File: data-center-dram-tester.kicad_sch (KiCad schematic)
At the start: 6 parts

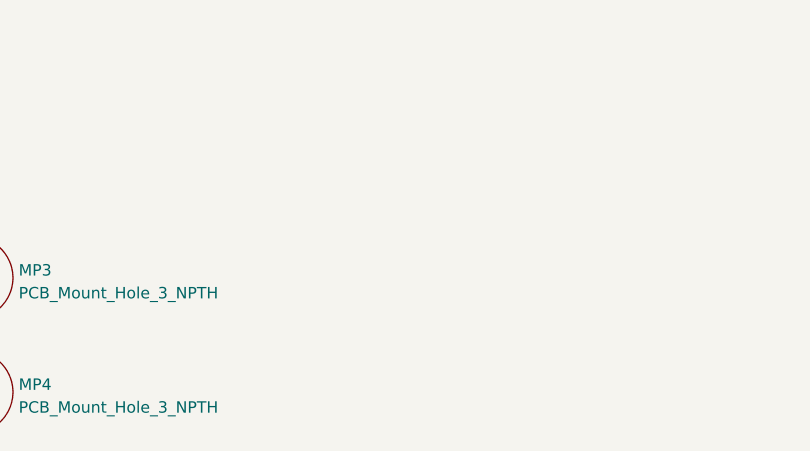
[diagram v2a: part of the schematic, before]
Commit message: Finish mechanical concept, add active capacitor discharge circuit for all AP DC-DC, add pushbutton controler circuit
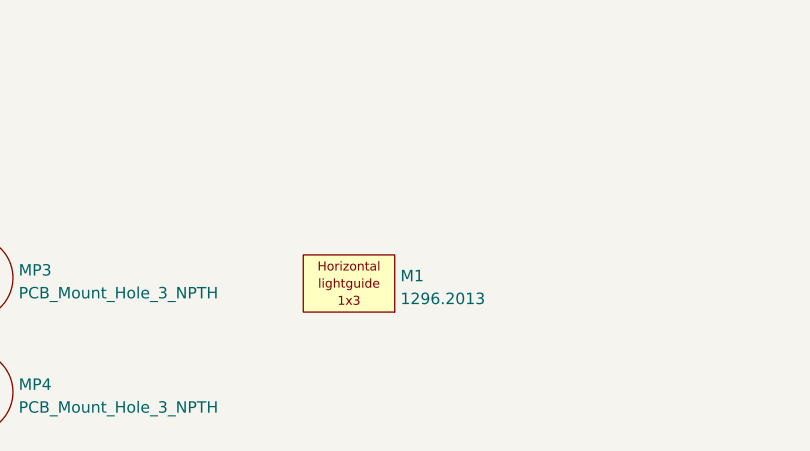
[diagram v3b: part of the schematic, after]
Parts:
- added M1: 1296.2013, antmicro-footprints:Mentor_1296.2013, symbol antmicroMechanicalParts:1296.2013

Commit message: Cleanup schematic
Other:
- sheet PCIe renamed FPGA banks 115-116
- moved on the sheet: N1, N2

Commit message: Add missing FMC vias, route: MODE, JTAG, active discharge, reconnect 5V buses
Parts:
- N1: footprint data-center-dram-tester-footprints:oshw-logo -> antmicro-footprints:OSHW-Logo_5.7x6mm_Mask
- N2: footprint data-center-dram-tester-footprints:antmicro-logo_scaled_20mm -> antmicro-footprints:antmicro-logo_scaled_20mm_mask
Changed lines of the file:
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@@
       (effects (font (size 1.27 1.27)) (justify left))
     )
-    (property "Footprint" "data-center-dram-tester-footprints:antmicro-logo_scaled_20mm" (id 2) (at 163.195 274.955 0)
+    (property "Footprint" "antmicro-footprints:antmicro-logo_scaled_20mm_mask" (id 2) (at 163.195 274.955 0)
       (effects (font (size 1.27 1.27)) hide)
     )
@@
       (effects (font (size 1.27 1.27)) (justify left))
     )
-    (property "Footprint" "data-center-dram-tester-footprints:oshw-logo" (id 2) (at 166.878 279.781 0)
+    (property "Footprint" "antmicro-footprints:OSHW-Logo_5.7x6mm_Mask" (id 2) (at 166.878 279.781 0)
       (effects (font (size 1.27 1.27)) hide)
     )
@@
       (reference "#PWR0370") (unit 1) (value "GND") (footprint "")
     )
+    (path "/00000000-0000-0000-0000-000060225b0c/e2d3e8d5-e790-456c-ac0a-688e96f2aeb5"
+      (reference "#PWR0371") (unit 1) (value "GND") (footprint "")
+    )
     (path "/00000000-0000-0000-0000-000060225b0c/00000000-0000-0000-0000-0000602c27ec"
       (reference "0V6") (unit 1) (value "TP_SMD1MM") (footprint "data-center-dram-tester-footprints:Testpoint_smd_1mm")
@@
       (reference "C283") (unit 1) (value "C_100n_0402") (footprint "antmicro-footprints:0402-cap")
     )
+    (path "/00000000-0000-0000-0000-000060225b0c/aef9ae6c-45c5-43c1-b158-f2635093852c"
+      (reference "C284") (unit 1) (value "C_100n_0402") (footprint "antmicro-footprints:0402-cap")
+    )
+    (path "/00000000-0000-0000-0000-000060225b0c/45d8bcaf-b136-41fb-adc6-0cee9f8462c1"
+      (reference "C285") (unit 1) (value "C_100n_0402") (footprint "antmicro-footprints:0402-cap")
+    )
     (path "/00000000-0000-0000-0000-00005f982999/39a2be85-a37e-4c79-aaee-d58056278055"
       (reference "C287") (unit 1) (value "C_100n_0402") (footprint "antmicro-footprints:0402-cap")
@@
     )
     (path "/00000000-0000-0000-0000-0000603b54ea"
-      (reference "N1") (unit 1) (value "oshw_logo") (footprint "data-center-dram-tester-footprints:oshw-logo")
+      (reference "N1") (unit 1) (value "oshw_logo") (footprint "antmicro-footprints:OSHW-Logo_5.7x6mm_Mask")
     )
     (path "/00000000-0000-0000-0000-00006003c9b5"
-      (reference "N2") (unit 1) (value "antmicro_logo") (footprint "data-center-dram-tester-footprints:antmicro-logo_scaled_20mm")
+      (reference "N2") (unit 1) (value "antmicro_logo") (footprint "antmicro-footprints:antmicro-logo_scaled_20mm_mask")
     )
     (path "/00000000-0000-0000-0000-000060225b0c/ecedd258-95de-47bb-aec8-b2c4683dacab"
